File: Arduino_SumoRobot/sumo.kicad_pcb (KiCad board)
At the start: 2 copper layers, 130.7 x 136.8 mm, 77 parts, among them IC1 40106D, K1 RELAY_C, K2 RELAY_C, K3 RELAY_C, K4 RELAY_C, P1 Power, P10 CONN_01X04, P11 CONN_01X04, P12 CONN_BATERIA12V, P13 CONN_01X02, P14 CONN_01X02, P17 CONN_01X02, P18 CONN_01X02, P19 CONN_02X16, P2 Analog, P3 Digital, P4 Digital, P5 CONN_1, P6 CONN_1, P7 CONN_1, P8 CONN_1, P9 CONN_01X06, Q1 S8050, Q2 S8050, Q3 S8050, Q4 S8050, U1 LM2576

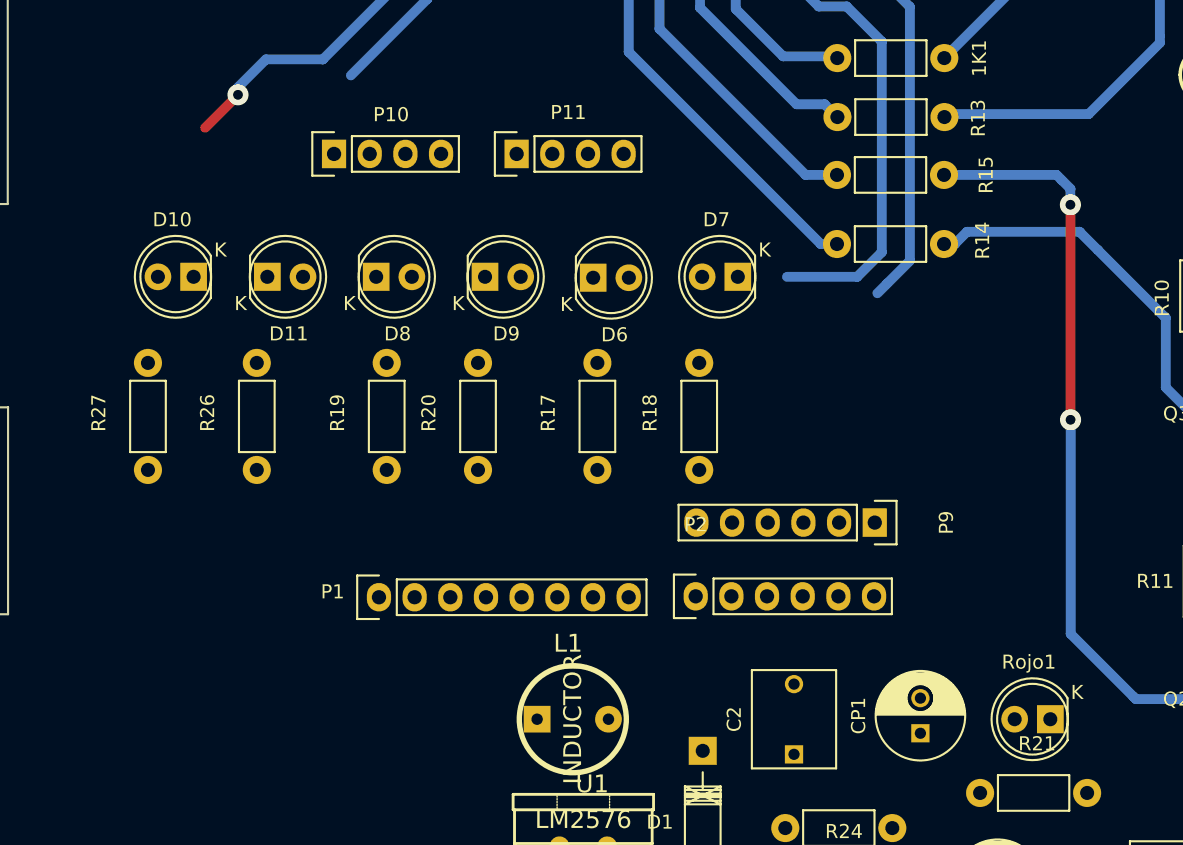
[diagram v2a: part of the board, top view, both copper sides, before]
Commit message: Arduino Sumo. Cambio todos los leds a 3mm porque había una mezcla.
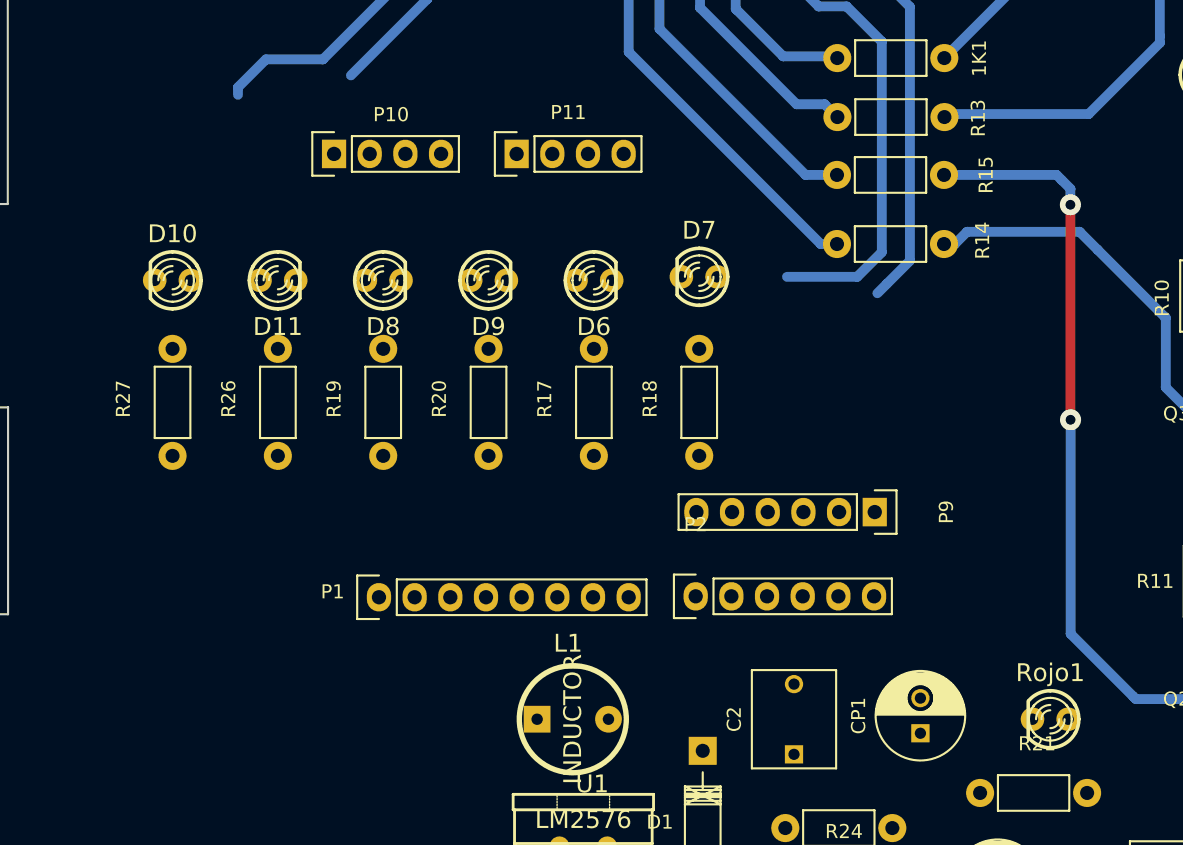
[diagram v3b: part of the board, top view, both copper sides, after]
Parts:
- D10, D11, D6, D7, D8, D9, Rojo1: footprint huellas:LED-5MM -> huellas:led-LED3MM
- moved D7 2.75 mm to (162.5, 92.2)
- moved R27 2.02 mm to (125.0, 105.0)
- moved R26 1.80 mm to (132.5, 105.0)
- moved D10 1.52 mm to (125.0, 92.5)
- moved R20 1.25 mm to (147.5, 105.0)
- moved R17 1.03 mm to (155.0, 105.0)
- moved R19 1.03 mm to (140.0, 105.0)
- moved R18 1.00 mm to (162.5, 105.0)
- moved D11 0.79 mm to (132.5, 92.5)
- moved P9 0.75 mm to (175.0, 109.0)
- moved D8 0.56 mm to (140.0, 92.5)
- moved D9 0.35 mm to (147.5, 92.5)
- moved D6 0.19 mm to (155.0, 92.5)
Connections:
- IC1 pad 10: Net-(D11-Pad1) -> Net-(D11-PadK)
- IC1 pad 12: Net-(D10-Pad1) -> Net-(D10-PadK)
- IC1 pad 6: Net-(D8-Pad1) -> Net-(D8-PadK)
- IC1 pad 8: Net-(D9-Pad1) -> Net-(D9-PadK)
- P3 pad 1: Net-(D10-Pad1) -> Net-(D10-PadK)
- P3 pad 2: Net-(D11-Pad1) -> Net-(D11-PadK)
- P3 pad 5: Net-(D8-Pad1) -> Net-(D8-PadK)
- P3 pad 6: Net-(D9-Pad1) -> Net-(D9-PadK)
- R17 pad 2: Net-(D6-Pad2) -> Net-(D6-PadA)
- R18 pad 2: Net-(D7-Pad2) -> Net-(D7-PadA)
- R19 pad 2: Net-(D8-Pad2) -> Net-(D8-PadA)
- R20 pad 2: Net-(D9-Pad2) -> Net-(D9-PadA)
- R26 pad 2: Net-(D11-Pad2) -> Net-(D11-PadA)
- R27 pad 2: Net-(D10-Pad2) -> Net-(D10-PadA)
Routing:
- net Net-(D9-PadK): track 0.00 -> 73.4 mm
- net Net-(D9-Pad1): track 73.4 -> 0.00 mm
- net Net-(D8-Pad1): track 65.4 -> 0.00 mm, vias 1 -> 0
- net Net-(D8-PadK): track 0.00 -> 62.1 mm

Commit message: Agrego mejoras al Arduino Sumo Robot realizadas por el Grupo II de 2016.
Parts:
- C2: value C -> 100nF
- CP1: value CP1 -> 10uF
- CP2: value CP1 -> 100uF
- D1: value D -> 1N5819
- L1: value INDUCTOR -> 330uHy
- P19: footprint huellas:Pin_Header_Straight_2x16_Pitch2.00mm -> Pin_Headers:Pin_Header_Straight_2x16
- R17, R18, R19, R20, R21, R23, R24: value R -> 1K
- moved P5 29.5 mm to (220.0, 32.0)
- moved P8 6.34 mm to (211.0, 138.0)
- moved P19 4.22 mm to (108.5, 41.8)
- moved P10 1.52 mm to (136.8, 82.0)
- moved P11 1.50 mm to (149.5, 82.0)
- moved R22 1.50 mm to (184.2, 37.5)
- moved R25 1.50 mm to (171.8, 37.5)
- moved P7 1.44 mm to (104.0, 60.0)
- moved R1 1.41 mm to (109.6, 34.1)
- moved R2 1.41 mm to (119.8, 34.1)
- moved R3 1.41 mm to (130.0, 34.1)
- moved R4 1.41 mm to (140.3, 34.1)
- moved R5 1.41 mm to (114.5, 26.5)
- moved R6 1.41 mm to (125.2, 26.5)
- moved R7 1.41 mm to (135.0, 26.4)
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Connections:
- P1 pad 1: (no net) -> Net-(P1-Pad1)
- P1 pad 2: (no net) -> Net-(P1-Pad2)
- P1 pad 3: (no net) -> Net-(P1-Pad3)
- P1 pad 4: (no net) -> Net-(P1-Pad4)
- P3 pad 3: (no net) -> Net-(P3-Pad3)
- P4 pad 7: (no net) -> Net-(P4-Pad7)
- P4 pad 8: (no net) -> Net-(P4-Pad8)
- P5 pad 1: (no net) -> Net-(P5-Pad1)
- P6 pad 1: (no net) -> Net-(P6-Pad1)
- P7 pad 1: (no net) -> Net-(P7-Pad1)
- P8 pad 1: (no net) -> Net-(P8-Pad1)
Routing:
- net GND: track 270.5 -> 712.1 mm, vias 11 -> 15
- net +5V: track 310.3 -> 608.9 mm, vias 0 -> 4
- net Net-(D11-PadK): track 0.00 -> 166.5 mm, vias 0 -> 2
- net Net-(D10-PadK): track 0.00 -> 118.0 mm, vias 0 -> 2
- net +12V: track 145.0 -> 215.7 mm
- net VCC: track 0.00 -> 62.3 mm
- net /2: track 46.3 -> 81.6 mm
- net Net-(D9-PadK): track 73.4 -> 107.2 mm
- net Net-(D1-Pad1): track 0.00 -> 29.9 mm
- net Net-(IC1-Pad11): track 0.00 -> 24.5 mm
- net Net-(D8-PadK): track 62.1 -> 84.2 mm
- net Net-(R23-Pad2): track 0.00 -> 18.4 mm
- net /11(**/MOSI): track 0.00 -> 17.9 mm
- net /10(**/SS): track 0.00 -> 17.9 mm
- net /3(**): track 51.9 -> 68.0 mm
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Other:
- board size 130.7 x 136.8 mm -> 132 x 125.8 mm
- board text removed: "EL BORDE DE IMPRESO NO CIERRA BIEN. ELEGIR GLRILLA 1MM Y REDIBUJAR BORDE."
- board text removed: "GND SE RUTEA AL FINAL"
- board text removed: "HASTA ACA HACER EL PCB"
- board text removed: "RUTEAR OTRA VEZ LA FUENTE INTENTAR RESPETAR LA UBICACION PROPUESTA (MOVIMIENTOS MINIMOS)"
